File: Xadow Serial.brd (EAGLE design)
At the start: 28.1 x 20.3 mm, 29 parts, among them J1 CONNECTOR-HEADER-8P-3461050P1, J2 12p 0.5mm bottom contact, J3 12p 0.5mm bottom contact, J4 12p 0.5mm bottom contact, SW2 ADDR, U1 SC16IS750, U2 BSS138PS, X1 CTS_32X25_SMD

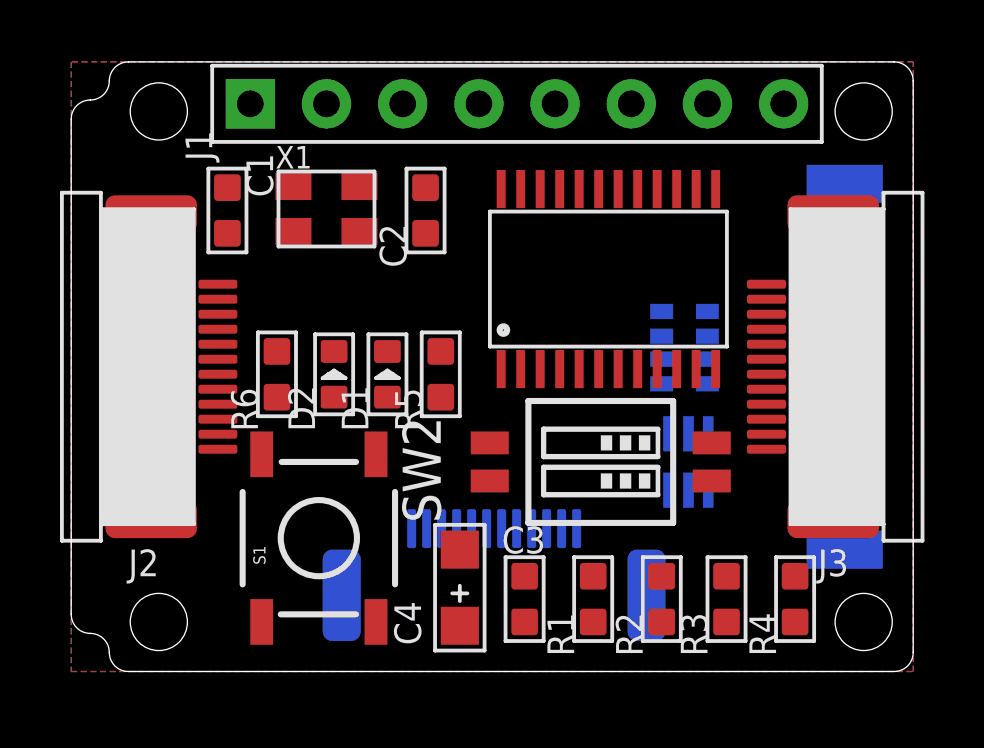
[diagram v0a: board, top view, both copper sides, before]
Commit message: Fully routed with solder jumpers
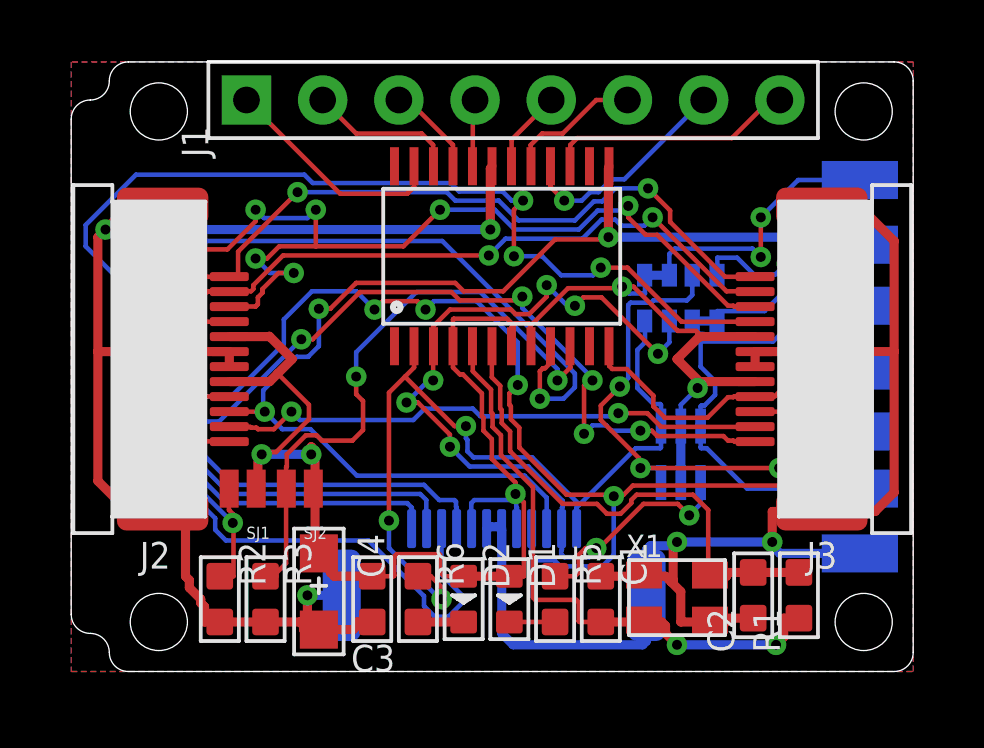
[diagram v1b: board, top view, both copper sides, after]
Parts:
- removed R4: 1K, OPL:R0603
- removed S1: TAC_SWITCHSMD, SparkFun-Electromechanical:TACTILE-SWITCH-SMD
- removed SW2: ADDR, SparkFun-Electromechanical:DIPSWITCH-02-50MIL
- added SJ1, SJ2: JUMPER-PAD-2-NO, SparkFun-Passives:PAD-JUMPER-2-NO_NO_SILK
- R7: value (none) -> 10K
- moved C1 18.0 mm to (17.8, 2.54)
- moved X1 17.4 mm to (20.3, 2.54)
- moved C2 16.8 mm to (22.9, 2.67)
- moved R3 15.4 mm to (6.60, 2.54), turned to 270 degrees
- moved R2 14.7 mm to (5.08, 2.54), turned to 270 degrees
- moved R6 8.84 mm to (11.7, 2.54), turned to 270 degrees
- moved D2 8.65 mm to (13.2, 2.54), turned to 270 degrees
- moved D1 8.52 mm to (14.7, 2.54), turned to 270 degrees
- moved R5 8.41 mm to (16.3, 2.54), turned to 270 degrees
- moved GND 8.14 mm to (26.4, 4.06)
- moved SDA 8.14 mm to (26.4, 12.3)
- moved R1 6.86 mm to (24.4, 2.67)
- moved C3 5.08 mm to (10.2, 2.54), turned to 90 degrees
- moved C4 4.70 mm to (8.38, 2.79), turned to 270 degrees
- moved SCL 4.10 mm to (26.4, 10.2)
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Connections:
- removed net N$17: C3.1, C4.-
- removed net N$5: R4.2, S1.4, U1.P$4
- net 3V3: now also SJ1.1, SJ2.1, U1.P$4; no longer R4.1, SW2.3, SW2.4
- net GND: now also C3.1, C4.-; no longer S1.2
- net N$3: now also SJ2.2; no longer SW2.1
- net N$4: now also SJ1.2; no longer SW2.2
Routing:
- net GND: track 0.00 -> 93.1 mm, vias 0 -> 5
- net 3V3: track 0.00 -> 69.7 mm, vias 0 -> 7
- net PB3/D14/MISO: track 0.00 -> 54.2 mm, vias 0 -> 7
- net PD0/SCL/D3: track 0.00 -> 49.0 mm, vias 0 -> 6
- net PF0/A5: track 0.00 -> 48.3 mm, vias 0 -> 5
- net PD1/SDA/D2: track 0.00 -> 45.8 mm, vias 0 -> 6
- net PB1/D15/SCK: track 0.00 -> 38.6 mm, vias 0 -> 3
- net PB2/D16/MOSI: track 0.00 -> 36.4 mm, vias 0 -> 3
- net N$4: track 0.00 -> 32.7 mm, vias 0 -> 2
- net RX: track 0.00 -> 31.0 mm, vias 0 -> 8
- net TX: track 0.00 -> 28.1 mm, vias 0 -> 3
- net PD3/TXO/D1: track 0.00 -> 26.3 mm, vias 0 -> 6
- net N$3: track 0.00 -> 20.6 mm, vias 0 -> 2
- net N$1: track 0.00 -> 20.0 mm, vias 0 -> 2
- net RX_5: track 0.00 -> 19.0 mm, vias 0 -> 2
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
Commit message: Fixed up labels
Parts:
- renumbered SJ1 to A0, SJ2 to A1
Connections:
- net N$11 renamed IO4
- net N$12 renamed IO5
- net N$13 renamed IO6
- net N$14 renamed IO7
- net N$6 renamed IO0
- net N$7 renamed IO1
- net N$8 renamed IO2
- net N$9 renamed IO3
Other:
- board text added: "IO0"
- board text added: "IO1"
- board text added: "IO2"
- board text added: "IO3"
- board text added: "IO4"
- board text added: "IO5"
- board text added: "IO6"
- board text added: "IO7"
